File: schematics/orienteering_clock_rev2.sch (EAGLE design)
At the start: 59 parts, among them IC1 TPIC6B595N, IC2 TPIC6B595N, J2 ICSP, Q1 IRFU9024V, Q2 IRFU9024V, Q3 IRFU9024V, Q4 IRFU9024V, Q5 IRFU9024V, Q6 IRFU9024V, T1 BC547, U3 ATMEGA328, Y2 16MHz

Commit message: schematics: cosmetic changes
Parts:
- renumbered MOD1 to VIN_REG1
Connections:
- net +12V: no longer BUZZ1.+
- net 5V: no longer VIN_REG1.SHDN, VIN_REG1.VOUT
- net VCC: now also VIN_REG1.SHDN, VIN_REG1.VOUT
- net VIN: now also BUZZ1.+, VIN_REG1.VIN
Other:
- note added: "TODO: - dot point in the middle of big displays - add POWER source flow - measure BATTERY voltage? - add buttons (connectors?) - add necessary connectors..."
- note removed: "TODO: - dot point in the middle of big displays - add POWER source - measure BATTERY voltage? - add necessary connectors..."
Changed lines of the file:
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@@
 <part name="C_LG" library="wirepad" deviceset="1,6/0,9" device=""/>
 <part name="BUZZ1" library="buzzer" deviceset="F/BC40" device=""/>
-<part name="P+6" library="supply1" deviceset="+12V" device=""/>
 <part name="T1" library="transistor" deviceset="BC547" device=""/>
 <part name="GND1" library="supply1" deviceset="GND" device=""/>
@@
 <part name="C4" library="SparkFun-Capacitors" deviceset="CAP" device="PTH" value="22pF"/>
 <part name="GND10" library="SparkFun" deviceset="GND" device=""/>
-<part name="MOD1" library="_hhn_Pololu" deviceset="POLOLU_D24V3F*" device="-HC" technology="5"/>
+<part name="VIN_REG1" library="_hhn_Pololu" deviceset="POLOLU_D24V3F*" device="-HC" technology="5"/>
 <part name="LED_SMALL_1" library="MINE" deviceset="7-SEG_" device="SA23-12SRWA"/>
 <part name="LED_SMALL_2" library="MINE" deviceset="7-SEG_" device="SA23-12SRWA"/>
@@
 <text x="281.94" y="71.12" size="1.778" layer="91">TODO:
  - dot point in the middle of big displays
- - add POWER source
+ - add POWER source flow
  - measure BATTERY voltage?
+ - add buttons (connectors?)
  - add necessary connectors...</text>
 <wire x1="-45.72" y1="7.62" x2="-45.72" y2="127" width="0.1524" layer="95" style="shortdash"/>
@@
 <attribute name="NAME" x="-20.32" y="-6.35" size="1.778" layer="95"/>
 </instance>
-<instance part="P+6" gate="1" x="-25.4" y="-10.16"/>
 <instance part="T1" gate="G$1" x="-15.24" y="-20.32" smashed="yes">
 <attribute name="NAME" x="-12.7" y="-20.32" size="1.778" layer="95"/>
@@
 </instance>
 <instance part="GND10" gate="1" x="88.9" y="73.66"/>
-<instance part="MOD1" gate="G$1" x="248.92" y="111.76"/>
+<instance part="VIN_REG1" gate="G$1" x="248.92" y="111.76"/>
 <instance part="LED_SMALL_1" gate="G$1" x="22.86" y="2.54"/>
 <instance part="LED_SMALL_2" gate="G$1" x="22.86" y="-30.48"/>
@@
 </segment>
 <segment>
-<pinref part="BUZZ1" gate="G$1" pin="+"/>
-<wire x1="-20.32" y1="-15.24" x2="-25.4" y2="-15.24" width="0.1524" layer="91"/>
-<pinref part="P+6" gate="1" pin="+12V"/>
-<wire x1="-25.4" y1="-15.24" x2="-25.4" y2="-12.7" width="0.1524" layer="91"/>
-</segment>
-<segment>
 <pinref part="P+7" gate="1" pin="+12V"/>
 <pinref part="CONTROL1" gate="A" pin="10"/>
@@
 </segment>
 <segment>
-<pinref part="MOD1" gate="G$1" pin="GND"/>
+<pinref part="VIN_REG1" gate="G$1" pin="GND"/>
 <wire x1="264.16" y1="104.14" x2="269.24" y2="104.14" width="0.1524" layer="91"/>
 <wire x1="269.24" y1="104.14" x2="269.24" y2="101.6" width="0.1524" layer="91"/>
@@
 <pinref part="P+10" gate="VCC" pin="VCC"/>
 </segment>
+<segment>
+<pinref part="VIN_REG1" gate="G$1" pin="VOUT"/>
+<pinref part="VIN_REG1" gate="G$1" pin="SHDN"/>
+<wire x1="236.22" y1="104.14" x2="236.22" y2="93.98" width="0.1524" layer="91"/>
+<wire x1="236.22" y1="93.98" x2="274.32" y2="93.98" width="0.1524" layer="91"/>
+<wire x1="274.32" y1="93.98" x2="274.32" y2="116.84" width="0.1524" layer="91"/>
+<wire x1="274.32" y1="116.84" x2="264.16" y2="116.84" width="0.1524" layer="91"/>
+<wire x1="274.32" y1="116.84" x2="281.94" y2="116.84" width="0.1524" layer="91"/>
+<junction x="274.32" y="116.84"/>
+<label x="281.94" y="116.84" size="1.27" layer="95" xref="yes"/>
+</segment>
 </net>
 <net name="N$1" class="0">
@@
 <segment>
 <pinref part="T1" gate="G$1" pin="B"/>
-<wire x1="-17.78" y1="-20.32" x2="-20.32" y2="-20.32" width="0.1524" layer="91"/>
-<label x="-20.32" y="-20.32" size="1.27" layer="95" rot="MR0" xref="yes"/>
+<wire x1="-17.78" y1="-20.32" x2="-22.86" y2="-20.32" width="0.1524" layer="91"/>
+<label x="-22.86" y="-20.32" size="1.27" layer="95" rot="MR0" xref="yes"/>
 </segment>
 </net>
@@
 <wire x1="182.88" y1="157.48" x2="185.42" y2="157.48" width="0.1524" layer="91"/>
 <wire x1="182.88" y1="157.48" x2="182.88" y2="165.1" width="0.1524" layer="91"/>
-</segment>
-<segment>
-<pinref part="MOD1" gate="G$1" pin="VOUT"/>
-<pinref part="MOD1" gate="G$1" pin="SHDN"/>
-<wire x1="236.22" y1="104.14" x2="236.22" y2="93.98" width="0.1524" layer="91"/>
-<wire x1="236.22" y1="93.98" x2="274.32" y2="93.98" width="0.1524" layer="91"/>
-<wire x1="274.32" y1="93.98" x2="274.32" y2="116.84" width="0.1524" layer="91"/>
-<wire x1="274.32" y1="116.84" x2="264.16" y2="116.84" width="0.1524" layer="91"/>
-<wire x1="274.32" y1="116.84" x2="281.94" y2="116.84" width="0.1524" layer="91"/>
-<junction x="274.32" y="116.84"/>
-<label x="281.94" y="116.84" size="1.27" layer="95" xref="yes"/>
 </segment>
 </net>
@@
 <wire x1="177.8" y1="149.86" x2="177.8" y2="152.4" width="0.1524" layer="91"/>
 </segment>
-</net>
+<segment>
+<pinref part="VIN_REG1" gate="G$1" pin="VIN"/>
+<wire x1="236.22" y1="116.84" x2="233.68" y2="116.84" width="0.1524" layer="91"/>
+<label x="233.68" y="116.84" size="1.27" layer="95" rot="MR0" xref="yes"/>
+</segment>
+<segment>
+<pinref part="BUZZ1" gate="G$1" pin="+"/>
+<wire x1="-20.32" y1="-15.24" x2="-22.86" y2="-15.24" width="0.1524" layer="91"/>
+<label x="-22.86" y="-15.24" size="1.27" layer="95" rot="MR0" xref="yes"/>
+</segment>
+</net>

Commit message: schematics: 2.0 schematics done
add: PDF printout of the 2.0 schematics
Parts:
- removed A_B1, A_B2, A_B3, A_B4, C_LA, C_LB, C_LC, C_LD, C_LE, C_LF, C_LG: (no value), wirepad:1,6/0,9
- removed BUZZ1: F/BC40, buzzer:F/BC40
- removed CONTROL1: JP_1, pinhead:PINHD-2X5
- removed JP10: (no value), SparkFun-Connectors:M08LOCK
- added JP1: POWER_IN, SparkFun-Connectors:M03POLAR
- added JP3: BUZZER, SparkFun-Connectors:M02POLAR
- added JP4: BUTTONS, SparkFun-Connectors:M06LONGPADS
- added JP5: LED_CATHODE, SparkFun-Connectors:M08
- added JP6: LED_ANODE, SparkFun-Connectors:M04PTH
- added JP7: FTDI_DEVICE, SparkFun-Connectors:FTDI_DEVICE
- added R21: 560R, resistor:R-US_0207/12
- added R23: 1M, resistor:R-US_0204/5
- added R24: 220k, resistor:R-US_0204/5
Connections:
- removed net +12V: CONTROL1.10, Q1.S, Q2.S, Q3.S, Q4.S, Q5.S, Q6.S, R1.2, R2.2, R3.2, R4.2, R5.2, R6.2
- removed net 3.3V: JP10.5
- removed net 5V: JP10.4, JP10.7
- removed net BUZZ_CTL: CONTROL1.6
- removed net G: CONTROL1.8
- removed net N$1: A_B1.P, Q1.D
- removed net N$12: A_B4.P, Q4.D
- removed net N$2: BUZZ1.-, T1.C
- removed net N$4: A_B2.P, Q2.D
- removed net N$9: A_B3.P, Q3.D
- removed net RCK: CONTROL1.3
- removed net SER_IN: CONTROL1.7
- removed net SRCK: CONTROL1.1
- new net A_B1: JP6.1, Q1.D
- new net A_B2: JP6.2, Q2.D
- new net A_B3: JP6.3, Q3.D
- new net A_B4: JP6.4, Q4.D
- new net BUZZ_-: JP3.1, T1.C
- new net D7: IC1A.D7, R21.1
- new net DISP_12V: JP1.2, Q1.S, Q2.S, Q3.S, Q4.S, Q5.S, Q6.S, R1.2, R2.2, R3.2, R4.2, R5.2, R6.2
- new net L_DP: JP5.8, R21.2
- net AD0: now also R23.1, R24.2
- net DTR: now also JP7.DTR
- net GND: now also JP1.3, JP4.1, JP7.CTS, JP7.GND, R24.1; no longer CONTROL1.9, JP10.2, JP10.3
- net IO2: now also T1.B
- net IO3: now also JP4.6; no longer T1.B
- net IO4: now also JP4.5
- net IO5: now also JP4.4
- net IO6: now also JP4.3
- net IO7: now also JP4.2
- net L_A: now also JP5.1; no longer C_LA.P
- net L_B: now also JP5.2; no longer C_LB.P
- net L_C: now also JP5.3; no longer C_LC.P
- net L_D: now also JP5.4; no longer C_LD.P
- net L_E: now also JP5.5; no longer C_LE.P
- net L_F: now also JP5.6; no longer C_LF.P
- net L_G: now also JP5.7; no longer C_LG.P
- net RESET: no longer JP10.6
- net RX-I: now also JP7.TXO
- net TX-O: now also JP7.RXI
- net VCC: now also JP7.VCC; no longer CONTROL1.5
- net VIN: now also JP1.1, JP3.2, R23.2; no longer BUZZ1.+, JP10.1
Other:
- note added: "2 SMALLER 7-LEDS SOLDERED INTO IT"
- note added: "BTN_SET BTN_UP BTN_DOWN BTN_MODE BTN_BATT GND"
- note added: "CONTROLLER PCB"
- note added: "DISPLAY"
- note added: "POWER"
- note added: "Set IO2 to HIGH to enable BUZZER"
- note added: "TODO: - VCC/GND connector"
- note added: "VOLTAGE DIVIDER for measuring VIN voltage takes upto 27V"
- note removed: "TODO: - dot point in the middle of big displays - add POWER source flow - measure BATTERY voltage? - add buttons (connectors?) - add necessary connectors..."
- moved on the sheet: AD, C1, C2, C3, C4, C8, IC1, IC2, IOL, J2, JP2, LED_SMALL_1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

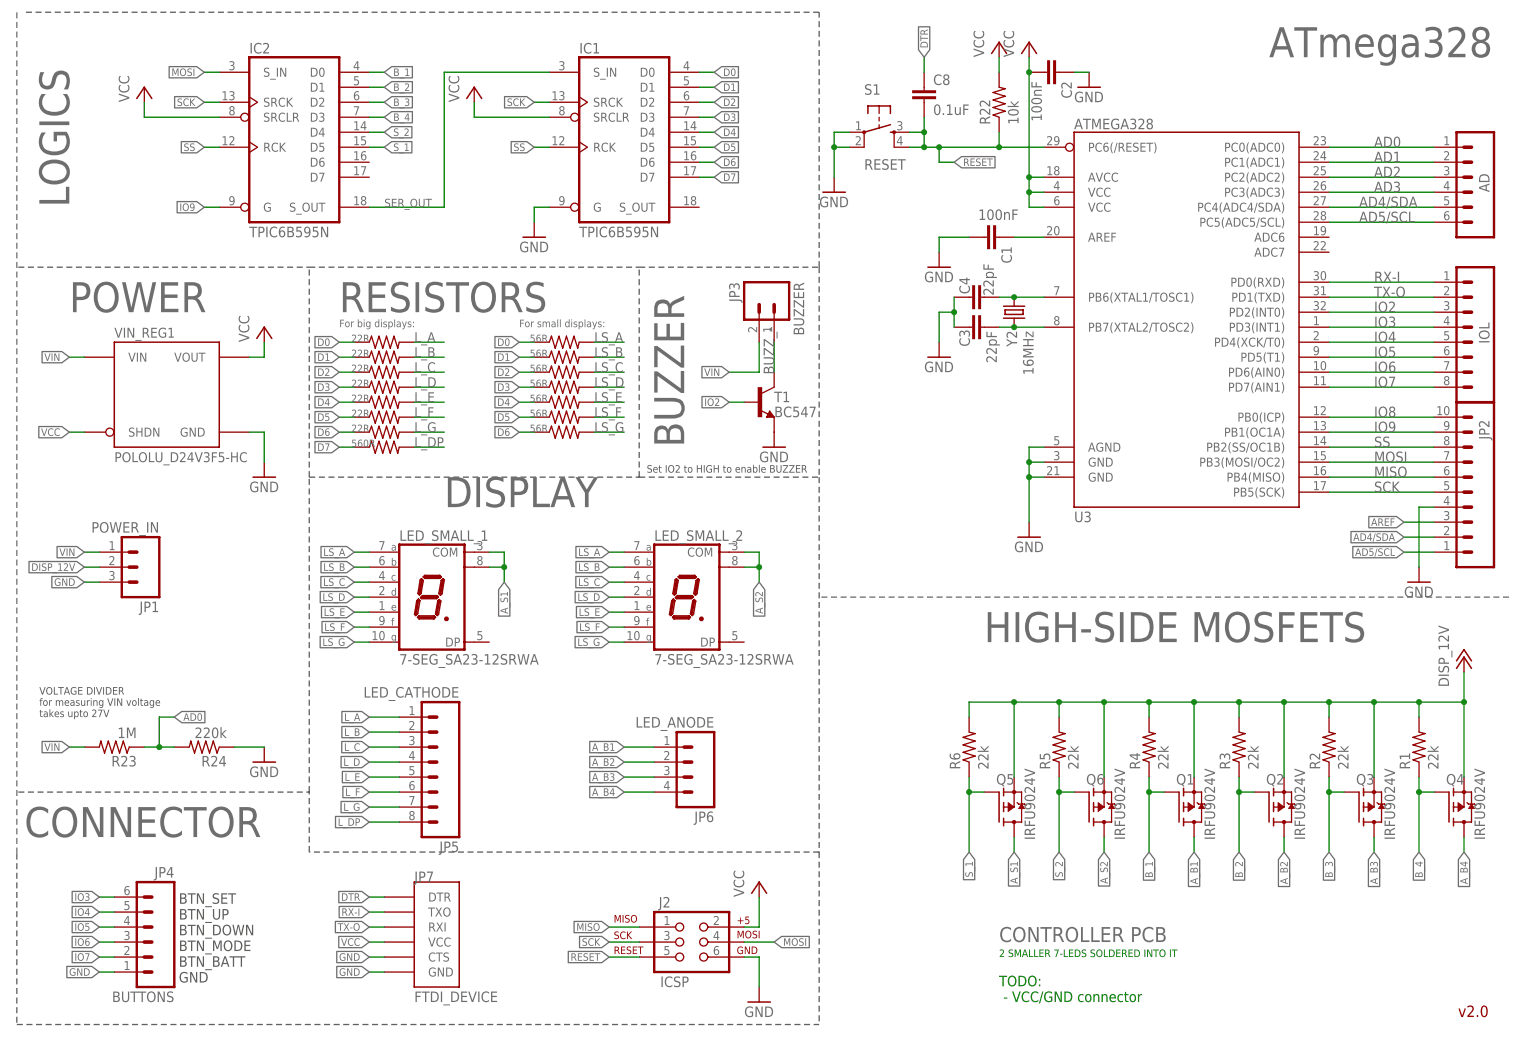
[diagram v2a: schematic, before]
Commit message: schematics:  first attempt at making a board
changes:
- removed BUTTONS connector (we will use the standard one)
- added net classes
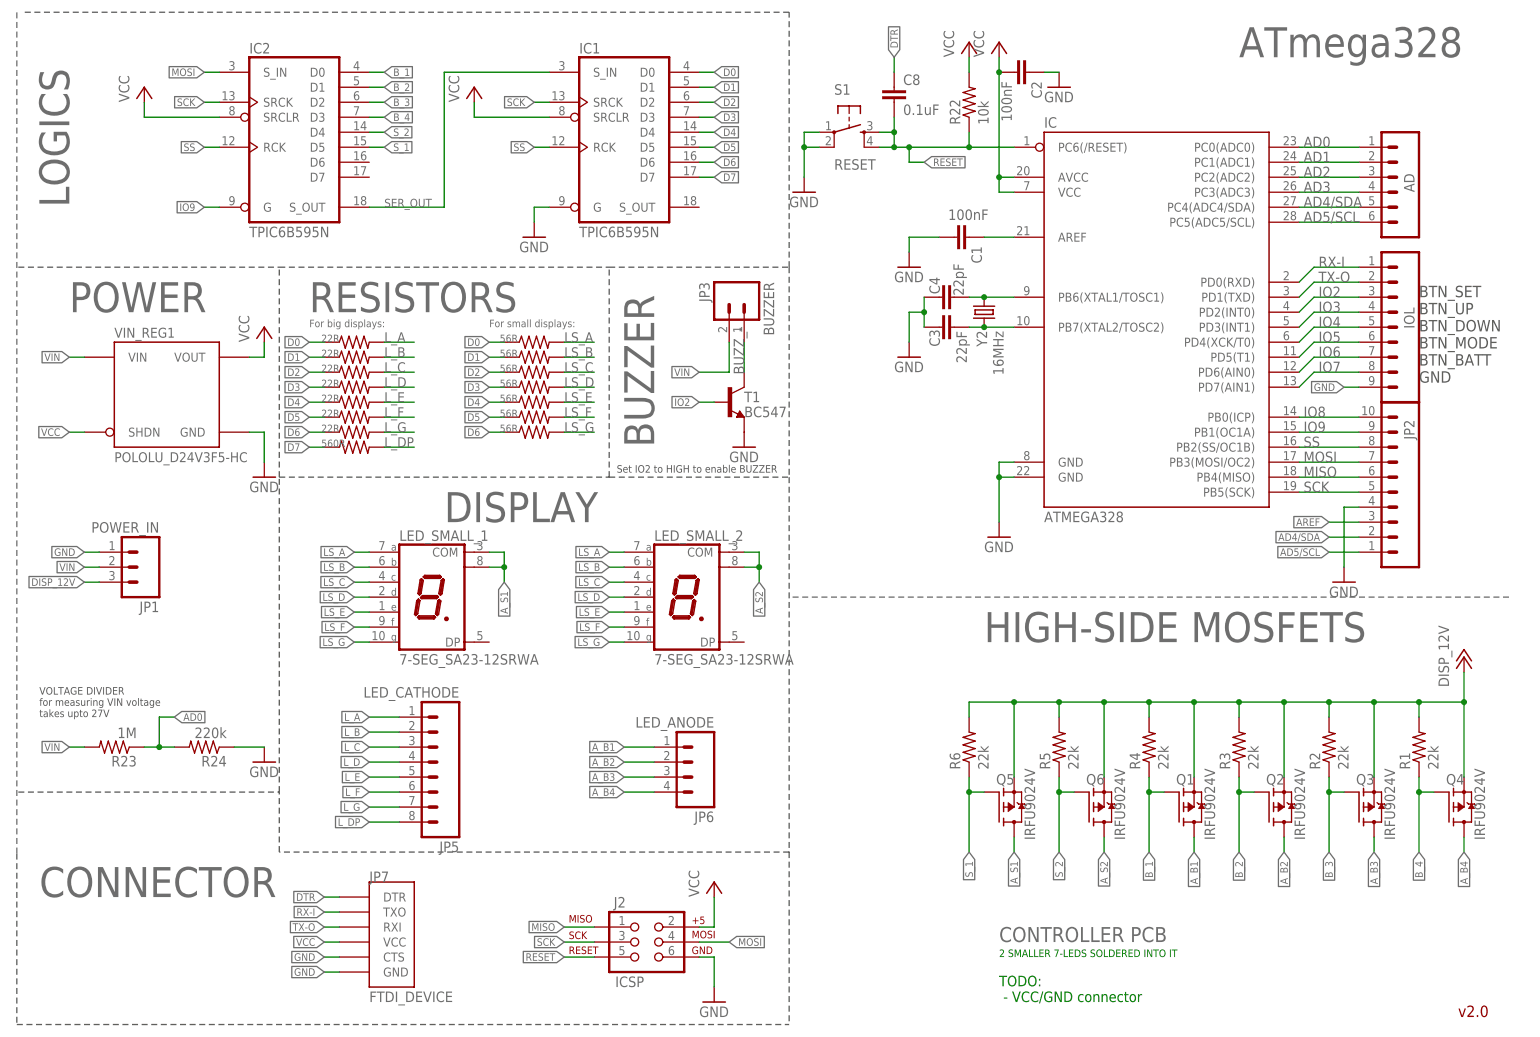
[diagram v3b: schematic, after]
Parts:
- removed JP4: BUTTONS, SparkFun-Connectors:M06LONGPADS
- removed U3: ATMEGA328, SparkFun:ATMEGA168
- added IC: ATMEGA328, SparkFun-DigitalIC:ATMEGA328P_PDIP
- IOL: value (none) -> M09LOCK; device SparkFun:M08LOCK -> SparkFun-Connectors:M09LOCK
- R22: device SparkFun:RESISTOR0603-RES -> resistor:R-US_0207/10
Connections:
- net AD0: now also IC.PC0(ADC0); no longer U3.PC0(ADC0)
- net AD1: now also IC.PC1(ADC1); no longer U3.PC1(ADC1)
- net AD2: now also IC.PC2(ADC2); no longer U3.PC2(ADC2)
- net AD3: now also IC.PC3(ADC3); no longer U3.PC3(ADC3)
- net AD4/SDA: now also IC.PC4(ADC4/SDA); no longer U3.PC4(ADC4/SDA)
- net AD5/SCL: now also IC.PC5(ADC5/SCL); no longer U3.PC5(ADC5/SCL)
- net AREF: now also IC.AREF; no longer U3.AREF
- net DISP_12V: now also JP1.3; no longer JP1.2
- net GND: now also IC.GND@1, IC.GND@2, IOL.9, JP1.1; no longer JP1.3, JP4.1, U3.AGND, U3.GND@1, U3.GND@2
- net IO2: now also IC.PD2(INT0); no longer U3.PD2(INT0)
- net IO3: now also IC.PD3(INT1); no longer JP4.6, U3.PD3(INT1)
- net IO4: now also IC.PD4(XCK/T0); no longer JP4.5, U3.PD4(XCK/T0)
- net IO5: now also IC.PD5(T1); no longer JP4.4, U3.PD5(T1)
- net IO6: now also IC.PD6(AIN0); no longer JP4.3, U3.PD6(AIN0)
- net IO7: now also IC.PD7(AIN1); no longer JP4.2, U3.PD7(AIN1)
- net IO8: now also IC.PB0(ICP); no longer U3.PB0(ICP)
- net IO9: now also IC.PB1(OC1A); no longer U3.PB1(OC1A)
- net MISO: now also IC.PB4(MISO); no longer U3.PB4(MISO)
- net MOSI: now also IC.PB3(MOSI/OC2); no longer U3.PB3(MOSI/OC2)
- net N$5: now also IC.PB6(XTAL1/TOSC1); no longer U3.PB6(XTAL1/TOSC1)
- net N$6: now also IC.PB7(XTAL2/TOSC2); no longer U3.PB7(XTAL2/TOSC2)
- net RESET: now also IC.PC6(/RESET); no longer U3.PC6(/RESET)
- net RX-I: now also IC.PD0(RXD); no longer U3.PD0(RXD)
- net SCK: now also IC.PB5(SCK); no longer U3.PB5(SCK)
- net SS: now also IC.PB2(SS/OC1B); no longer U3.PB2(SS/OC1B)
- net TX-O: now also IC.PD1(TXD); no longer U3.PD1(TXD)
- net VCC: now also IC.AVCC, IC.VCC; no longer U3.AVCC, U3.VCC@1, U3.VCC@2
- net VIN: now also JP1.2; no longer JP1.1
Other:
- moved on the sheet: AD, C1, C2, C3, C4, C8, J2, JP2, JP3, JP7, R22, S1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
